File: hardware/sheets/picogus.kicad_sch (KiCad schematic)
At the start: 59 parts, among them J1 IRQDMA_JP, J5 SWD, SW1 BOOTSEL, U1 RP2040, U10 74LVC2G06, U11 APS6404L, U12 PCM5102A, U2 W25Q128JVS, U3 AMS1117-3.3, U4 CB3T3257, U5 CB3T3257, U6 CB3T3245, U7 74AHC14, U8 74LVC00, U9 74LVC00, Y1 12MHz

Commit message: Design-review fixes: reset parking, IRQ8 off the header, analog cleanups
Netlist-wide review sweep. IRQ8 leaves the 60-pin ISA header (pin 15 is a
second GND return; the on-board RTC owns IRQ8 exclusively, so its push-pull
drive is now correct by construction). Bus MCU Hi-Z parking completed:
~CPURESET pulled low (V20 held in reset while the MCU is unprogrammed),
~DACK1/~REFRESH parked deasserted, DRQ1 idled low. Supervisor 12 MHz crystal
damping R actually in series now (was parallel-to-nothing), plus a second
USBLC6 so both prog-port SW2 positions are ESD-protected. Audio: 0.5x PG
summing (MCP6002 headroom), 100k LINE bleed, unit B parked as a follower --
and the SUM stub moved off pin 5's row, where wiring unit B would have
silently merged SUM into VREF. CH224K VDD fed through 1k per the WCH ref
design. VGA blue ladder rescaled 1k/510 -> 820/470 (was ~12% blue-deficient).
Spare CMOS gate inputs grounded uniformly (cpu_core/rtc/storage); UART_RXD
pulled up (SIN idles at mark with JP1 open); dead pins/parts dropped
(com_port CLK, parallel RESET_DRV, storage R3). Bus CLK fixed at 7.16 MHz
logged as a decision. New passives mapped to JLC basic parts in parts.py.

Co-Authored-By: Claude Fable 5 <noreply@anthropic.com>
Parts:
- R10, R11, R5: LCSC Part Num (none) -> C23179

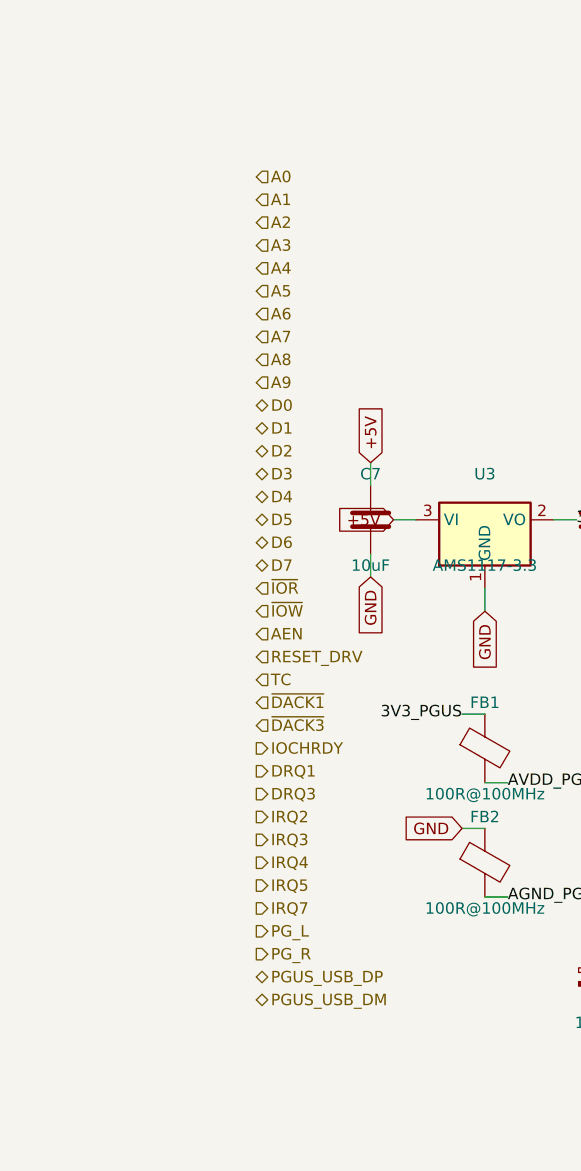
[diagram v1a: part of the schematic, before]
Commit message: ERC cleanup: NC flags on unused pins, anchored interface labels
KiCad 10 ERC drops from 366 to 16 violations, all noise:

- NC flags on the 36 genuinely unused pins (cpu_core '138/'161 spares,
  Supervisor RP2040 unused GPIO, Core2350B GPIO44-47, rtc '138 spares).
- emit_interface anchors every hier label on a stub wire ending in a
  same-name local label -- connectivity unchanged (still by name;
  netlist spans verified), but nothing dangles.
- Interface honesty: cpu_core drops AEN/IOCHRDY from PINS (both live on
  bus_mcu; nothing here touched them), bus_mcu drops PRIV_COUNTER (the
  counter chain is on-sheet, CNT_* never crosses).
- Remaining 6 label_dangling are root IRQ9-13/15: single-sheet by
  design (soft-PIC pull-ups await future 16-bit sources); kept in PINS
  as the AT-style contract.

Co-Authored-By: Claude Fable 5 <noreply@anthropic.com>
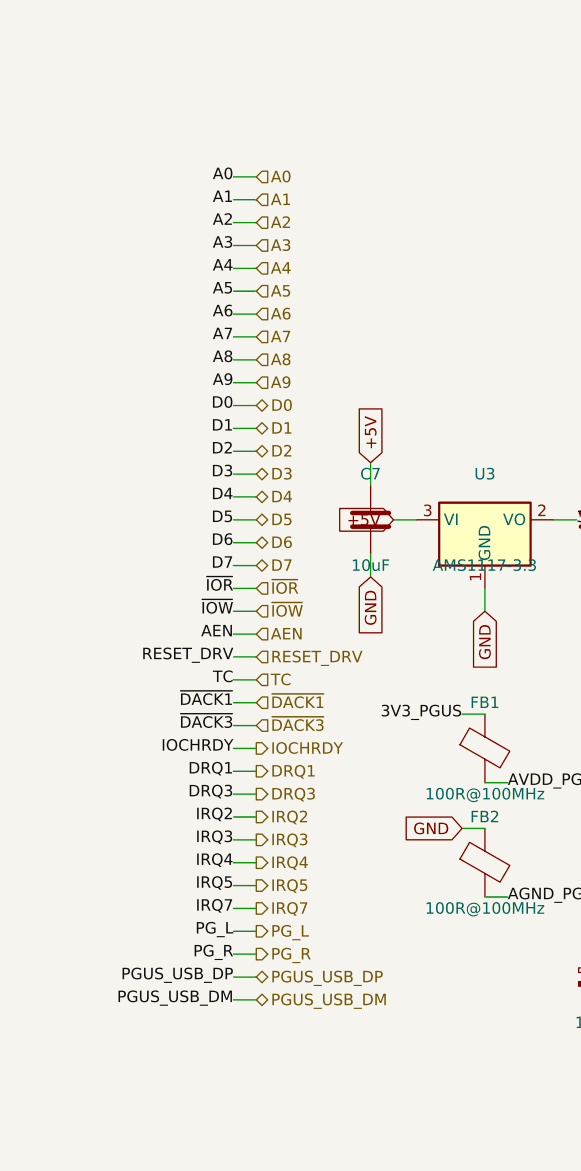
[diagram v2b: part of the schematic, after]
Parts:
- removed C3: 100nF, symbol Device:C
- removed R2: 1k, symbol Device:R
- removed R3, R4: 27, symbol Device:R
- removed R7: 10k, symbol Device:R
- removed SW1: BOOTSEL, symbol Switch:SW_Push
- removed U2: W25Q128JVS, symbol Memory_Flash:W25Q128JVS
- removed Y1: 12MHz, symbol Device:Crystal
- added C10, C9: 47uF, symbol Device:C
- added C11, C12, C21: 100nF, symbol Device:C
- added FB1, FB2: 100R@100MHz, symbol Device:FerriteBead
- added U3: AMS1117-3.3, symbol Regulator_Linear:AMS1117-3.3
- C3: renamed from FB1; value 100R@100MHz -> 100nF; symbol Device:FerriteBead -> Device:C; LCSC Part Num C160981 -> C14663
- J5: renamed from C12; value 100nF -> SWD; symbol Device:C -> Connector_Generic:Conn_01x03; LCSC Part Num C14663 -> C2337
- R2: renamed from FB2; value 100R@100MHz -> 1k; symbol Device:FerriteBead -> Device:R; LCSC Part Num C160981 -> C21190
- R3: renamed from C10; value 47uF -> 27; symbol Device:C -> Device:R; LCSC Part Num C16780 -> C25190
- R4: renamed from C11; value 100nF -> 27; symbol Device:C -> Device:R; LCSC Part Num C14663 -> C25190
- R7: renamed from C21; value 100nF -> 10k; symbol Device:C -> Device:R; LCSC Part Num C14663 -> C25804
- SW1: renamed from C9; value 47uF -> BOOTSEL; symbol Device:C -> Switch:SW_Push; LCSC Part Num C16780 -> C318884
- U2: renamed from U3; value AMS1117-3.3 -> W25Q128JVS; symbol Regulator_Linear:AMS1117-3.3 -> Memory_Flash:W25Q128JVS; LCSC Part Num C6186 -> C97521
- Y1: renamed from J5; value SWD -> 12MHz; symbol Connector_Generic:Conn_01x03 -> Device:Crystal; LCSC Part Num C2337 -> C9002
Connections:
- net +5V: now also C9.1, U3.3 (VI); no longer SW1.1, U2.3 (VI)
- net 3V3_PGUS: now also U2.8 (VCC), C10.1, C11.1, C12.1, C21.1, FB1.1, U3.2 (VO); no longer J5.1, R3.1, R4.1, U2.2 (VO)
- net AGND_PGUS: now also FB2.2; no longer R2.2
- net AVDD_PGUS: now also FB1.2; no longer C3.2
- net GND: now also C3.2, J5.3 (Pin_3), U2.4 (GND), C10.2, C11.2, C12.2, C21.2, C9.2, FB2.1, U3.1 (GND); no longer J5.2, R2.1, R3.2, R4.2, R7.2, U2.1 (GND), Y1.3 (Pin_3)
- net PGUS_QSPI_SCLK: now also U2.6 (CLK)
- net PGUS_QSPI_SD0: now also U2.5 (DI/IO_{0})
- net PGUS_QSPI_SD1: now also U2.2 (DO/IO_{1})
- net PGUS_QSPI_SD2: now also U2.3 (~{WP}/IO_{2})
- net PGUS_QSPI_SD3: now also U2.7 (~{HOLD}/~{RESET}/IO_{3})
- net PGUS_QSPI_SS: now also R2.1, U2.1 (~{CS})
- net PGUS_SWCLK: now also J5.2 (Pin_2); no longer Y1.2 (Pin_2)
- net PGUS_SWDIO: now also J5.1 (Pin_1); no longer Y1.1 (Pin_1)
- net PGUS_USB_DM: now also R4.2
- net PGUS_USB_DP: now also R3.2
- net USB_DM_I: now also R4.1
- net USB_DP_I: now also R3.1
- net XIN: now also Y1.1
- net XTAL_OUT: now also Y1.2
- net ~{BUSOE}: now also R7.2
- net ~{USB_BOOT}: now also R2.2, SW1.1

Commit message: ERC power cleanup: single flag owner, flags on series-fed rails
Full-build ERC is now just the 6 expected IRQ9-13/15 label_dangling.

- Root's duplicate PWR_FLAGs removed from build.py: power.py #FLG1-3
  own +5V/+3V3/GND; the pair made flag-vs-flag pin_to_pin errors.
- PWR_FLAGs added on the local rails ERC can't see through a series
  part: VBUS_MCU / VBUS_VID (Schottky diode-OR), VBUS_KBD / HDMI_5V
  (polyfuse), CH224_VDD (1k per WCH ref), AVDD_PGUS / AGND_PGUS
  (ferrite beads).

Net membership verified unchanged: 821 nets, node-identical to HEAD.

Co-Authored-By: Claude Fable 5 <noreply@anthropic.com>
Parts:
- removed C21: 100nF, symbol Device:C
- removed R9: 15k, symbol Device:R
- added J1: IRQDMA_JP, symbol Connector_Generic:Conn_02x09_Odd_Even
- added U12: PCM5102A, symbol mini-xt:PCM5102A
- C21: renamed from U12; value PCM5102A -> 100nF; symbol mini-xt:PCM5102A -> Device:C; LCSC Part Num C107671 -> C14663
- R9: renamed from J1; value IRQDMA_JP -> 15k; symbol Connector_Generic:Conn_02x09_Odd_Even -> Device:R; LCSC Part Num C2333 -> C22809
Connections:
- net +5V: now also R9.1
- net 3V3_PGUS: now also C21.1, U12.17 (XSMT), U12.20 (DVDD); no longer C21.17 (XSMT), C21.20 (DVDD)
- net AGND_PGUS: now also U12.3 (CPGND), U12.9 (AGND); no longer C21.3 (CPGND), C21.9 (AGND)
- net AVDD_PGUS: now also U12.1 (CPVDD), U12.8 (AVDD); no longer C21.1 (CPVDD), C21.8 (AVDD)
- net BCK: now also U12.13 (BCK); no longer C21.13 (BCK)
- net CAPM: now also U12.4 (CAPM); no longer C21.4 (CAPM)
- net CAPP: now also U12.2 (CAPP); no longer C21.2 (CAPP)
- net DACK: now also R9.2, J1.14 (Pin_14), J1.18 (Pin_18); no longer R9.14 (Pin_14), R9.18 (Pin_18)
- net DAC_L: now also U12.6 (OUTL); no longer C21.6 (OUTL)
- net DAC_R: now also U12.7 (OUTR); no longer C21.7 (OUTR)
- net DIN: now also U12.14 (DIN); no longer C21.14 (DIN)
- net DRQ: now also J1.12 (Pin_12), J1.16 (Pin_16); no longer R9.12 (Pin_12), R9.16 (Pin_16)
- net DRQ1: now also J1.11 (Pin_11); no longer R9.11 (Pin_11)
- net DRQ3: now also J1.15 (Pin_15); no longer R9.15 (Pin_15)
- net GND: now also C21.2, U12.10 (DEMP), U12.11 (FLT), U12.12 (SCK), U12.16 (FMT), U12.19 (DGND); no longer C21.10 (DEMP), C21.11 (FLT), C21.12 (SCK), C21.16 (FMT), C21.19 (DGND)
- net IRQ: now also J1.10 (Pin_10), J1.2 (Pin_2), J1.4 (Pin_4), J1.6 (Pin_6), J1.8 (Pin_8); no longer R9.10 (Pin_10), R9.2 (Pin_2), R9.4 (Pin_4), R9.6 (Pin_6), R9.8 (Pin_8)
- net IRQ2: now also J1.1 (Pin_1); no longer R9.1 (Pin_1)
- net IRQ3: now also J1.3 (Pin_3); no longer R9.3 (Pin_3)
- net IRQ4: now also J1.5 (Pin_5); no longer R9.5 (Pin_5)
- net IRQ5: now also J1.7 (Pin_7); no longer R9.7 (Pin_7)
- net IRQ7: now also J1.9 (Pin_9); no longer R9.9 (Pin_9)
- net LDOO: now also U12.18 (LDOO); no longer C21.18 (LDOO)
- net LRCK: now also U12.15 (LRCK); no longer C21.15 (LRCK)
- net VNEG: now also U12.5 (VNEG); no longer C21.5 (VNEG)
- net ~{DACK1}: now also J1.13 (Pin_13); no longer R9.13 (Pin_13)
- net ~{DACK3}: now also J1.17 (Pin_17); no longer R9.17 (Pin_17)
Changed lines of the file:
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@@
 	(wire
 		(pts
+			(xy 12.7 12.7)
+			(xy 12.7 10.16)
+		)
+		(stroke
+			(width 0)
+			(type default)
+		)
+	)
+	(label "AVDD_PGUS"
+		(at 12.7 10.16 90)
+		(effects
+			(font
+				(size 1.27 1.27)
+			)
+		)
+	)
+	(wire
+		(pts
+			(xy 27.94 12.7)
+			(xy 27.94 10.16)
+		)
+		(stroke
+			(width 0)
+			(type default)
+		)
+	)
+	(label "AGND_PGUS"
+		(at 27.94 10.16 90)
+		(effects
+			(font
+				(size 1.27 1.27)
+			)
+		)
+	)
+	(wire
+		(pts
 			(xy 76.2 59.69)
 			(xy 76.2 57.15)
@@
 					(unit 1)
 				)
+			)
+		)
+	)
+	(symbol
+		(lib_id "power:PWR_FLAG")
+		(at 12.7 12.7 0)
+		(unit 1)
+		(exclude_from_sim no)
+		(in_bom yes)
+		(on_board yes)
+		(dnp no)
+		(fields_autoplaced yes)
+		(property "Reference" "#FLG1"
+			(at 12.7 7.62 0)
+			(effects
+				(font
+					(size 1.27 1.27)
+				)
+			)
+		)
+		(property "Value" "PWR_FLAG"
+			(at 12.7 17.78 0)
+			(effects
+				(font
+					(size 1.27 1.27)
+				)
+			)
+		)
+		(property "Footprint" ""
+			(at 12.7 12.7 0)
+			(effects
+				(font
+					(size 1.27 1.27)
+				)
+				(hide yes)
+			)
+		)
+		(pin "1"
+		)
+		(instances
+			(project "mini-xt"
+				(path "/26736c46-8b40-5460-874f-03596d17270c/24f7f9a0-9103-58fe-b668-a97e2ed2b567"
+					(reference "#FLG1301")
+					(unit 1)
+				)
+			)
+		)
+	)
+	(symbol
+		(lib_id "power:PWR_FLAG")
+		(at 27.94 12.7 0)
+		(unit 1)
+		(exclude_from_sim no)
+		(in_bom yes)
+		(on_board yes)
+		(dnp no)
+		(fields_autoplaced yes)
+		(property "Reference" "#FLG2"
+			(at 27.94 7.62 0)
+			(effects
+				(font
+					(size 1.27 1.27)
+				)
+			)
+		)
+		(property "Value" "PWR_FLAG"
+			(at 27.94 17.78 0)
+			(effects
+				(font
+					(size 1.27 1.27)
+				)
+			)
+		)
+		(property "Footprint" ""
+			(at 27.94 12.7 0)
+			(effects
+				(font
+					(size 1.27 1.27)
+				)
+				(hide yes)
+			)
+		)
+		(pin "1"
+		)
+		(instances
+			(project "mini-xt"
+				(path "/26736c46-8b40-5460-874f-03596d17270c/24f7f9a0-9103-58fe-b668-a97e2ed2b567"
+					(reference "#FLG1302")
+					(unit 1)
+				)

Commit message: Hardwire storage IRQ14 and PicoGUS IRQ5; drop their IRQ jumpers
- Storage JP3 deleted: INTRQ -> '125 -> IRQ14 directly (the soft PIC
  is AT-style anyway). Poll vs interrupt is an XTIDE UB per-controller
  config choice, safe with the line wired either way -- the tri-state
  driver is silent unless the drive asserts INTRQ. ~{IRQ5_OE} renamed
  ~{IRQ_OE} to match.
- PicoGUS IRQ jumper row deleted: the shifter output drives IRQ5
  directly -- the free line and now its sole driver; every personality
  works on IRQ5 and pgusinit sets the firmware to match, so the 5-row
  jumper bought nothing. J1 shrinks 2x9 -> 2x4 (DMA pairs only, ch1 is
  the only MCU-serviced channel); parts.py header entry follows.
- IRQ5 contention is now zero: the sidecar header is the only other
  possible driver.

Full-build ERC: 0 violations; cards build clean.

Co-Authored-By: Claude Fable 5 <noreply@anthropic.com>
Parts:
- removed C7, C8: 10uF, symbol Device:C
- removed D1: LED, symbol Device:LED
- removed J1: IRQDMA_JP, symbol Connector_Generic:Conn_02x09_Odd_Even
- removed R5: 470, symbol Device:R
- removed R6: 10k, symbol Device:R
- added C6: 100nF, symbol Device:C
- added J1: DMA_JP, symbol Connector_Generic:Conn_02x04_Odd_Even
- added J5: SWD, symbol Connector_Generic:Conn_01x03
- added R4: 27, symbol Device:R
- added U10: 74LVC2G06, symbol mini-xt:74LVC2G06
- added U3: AMS1117-3.3, symbol Regulator_Linear:AMS1117-3.3
- C7: renamed from C6; value 100nF -> 10uF; LCSC Part Num C14663 -> C15850
- C8: renamed from U3; value AMS1117-3.3 -> 10uF; symbol Regulator_Linear:AMS1117-3.3 -> Device:C; LCSC Part Num C6186 -> C15850
- D1: renamed from J5; value SWD -> LED; symbol Connector_Generic:Conn_01x03 -> Device:LED; LCSC Part Num C2337 -> (none)
- R5: renamed from R4; value 27 -> 470; LCSC Part Num C25190 -> C23179
- R6: renamed from U10; value 74LVC2G06 -> 10k; symbol mini-xt:74LVC2G06 -> Device:R; LCSC Part Num C52145914 -> C25804
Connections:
- net IRQ is gone; now on net IRQ5: U6.5 (2Y1)
- net +5V: now also C7.1, U3.3 (VI); no longer C8.3 (VI)
- net 3V3_PGUS: now also C8.1, U10.5 (VCC), U3.2 (VO); no longer C8.2 (VO), R6.5 (VCC)
- net DACK: now also J1.4 (Pin_4), J1.8 (Pin_8)
- net DRQ: now also J1.2 (Pin_2), J1.6 (Pin_6)
- net DRQ1: now also J1.1 (Pin_1)
- net DRQ3: now also J1.5 (Pin_5)
- net GND: now also C8.2, D1.1 (K), C6.2, J5.3 (Pin_3), U10.2 (GND), U10.3 (2A), U3.1 (GND); no longer C8.1 (GND), D1.3 (Pin_3), R6.3 (2A)
- net IOCHRDY: now also U10.6 (1Y); no longer R6.6 (1Y)
- net LED_A: now also R5.1
- net LED_RA: now also D1.2 (A), R5.2
- net PGUS_SWCLK: now also J5.2 (Pin_2); no longer D1.2 (Pin_2)
- net PGUS_SWDIO: now also J5.1 (Pin_1); no longer D1.1 (Pin_1)
- net PGUS_USB_DM: now also R4.2; no longer R5.2
- net RESET_DRV: now also R6.1
- net RIOCHRDY: now also U10.1 (1A); no longer R6.1 (1A)
- net USB_DM_I: now also R4.1; no longer R5.1
- net VCORE: now also C6.1; no longer C7.1
- net ~{DACK1}: now also J1.3 (Pin_3)
- net ~{DACK3}: now also J1.7 (Pin_7)
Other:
- note added: "DMA jumpers: one DRQ/DACK pair -- our Bus MCU services DMA ch1 ONLY, so jumper DRQ1/DACK1. IRQ hardwired to IRQ5 (the free line, sole driver); pgusinit sets the firmware to match."
- note removed: "IRQ/DMA jumpers: one IRQ row + one DRQ/DACK pair. Our Bus MCU services DMA ch1 ONLY -- jumper DRQ1/DACK1. IRQ5 free (storage default is IRQ14)."
- moved on the sheet: C7, R5
